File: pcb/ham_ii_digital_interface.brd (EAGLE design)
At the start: 63.5 x 52.7 mm, 21 parts, among them IC1 LM358N, T1 Left Driver, T2 Brake Driver, T3 Right Driver

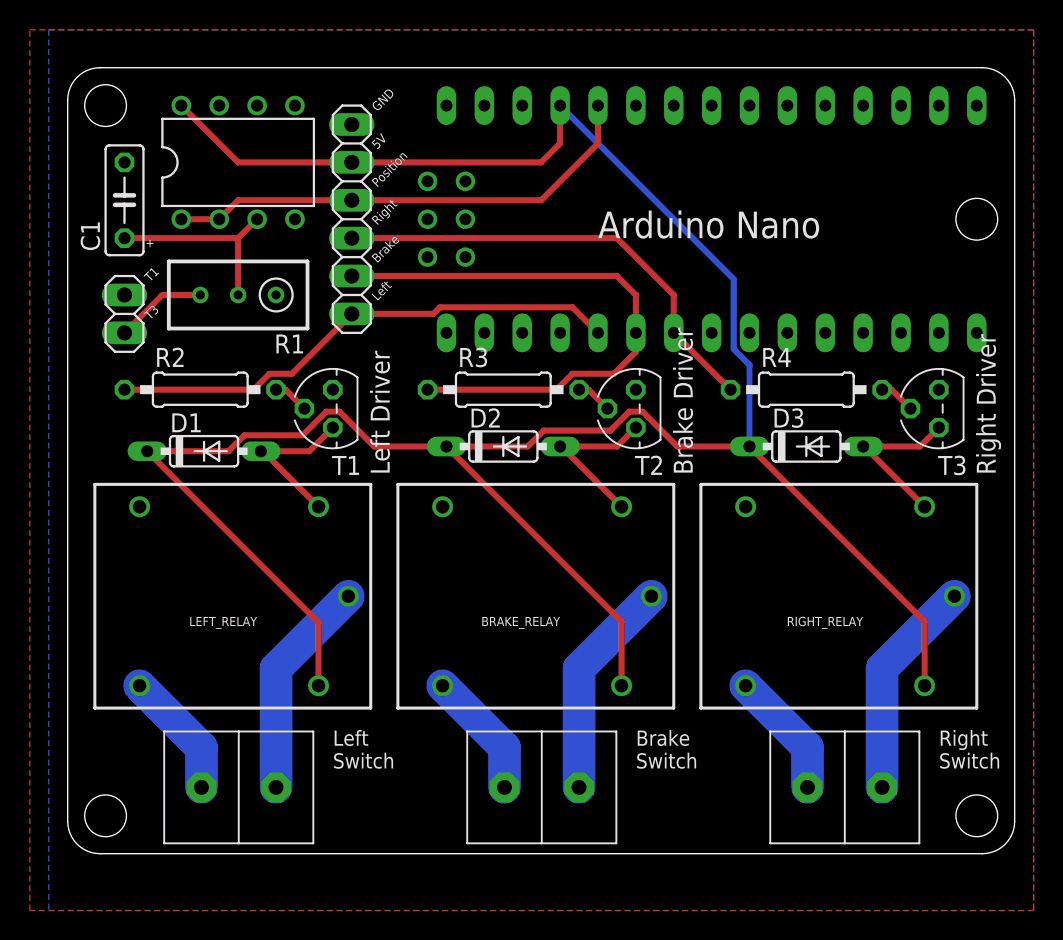
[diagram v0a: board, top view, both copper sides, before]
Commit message: Changed value of C1 and changed C1 to an electrolytic capacitor.
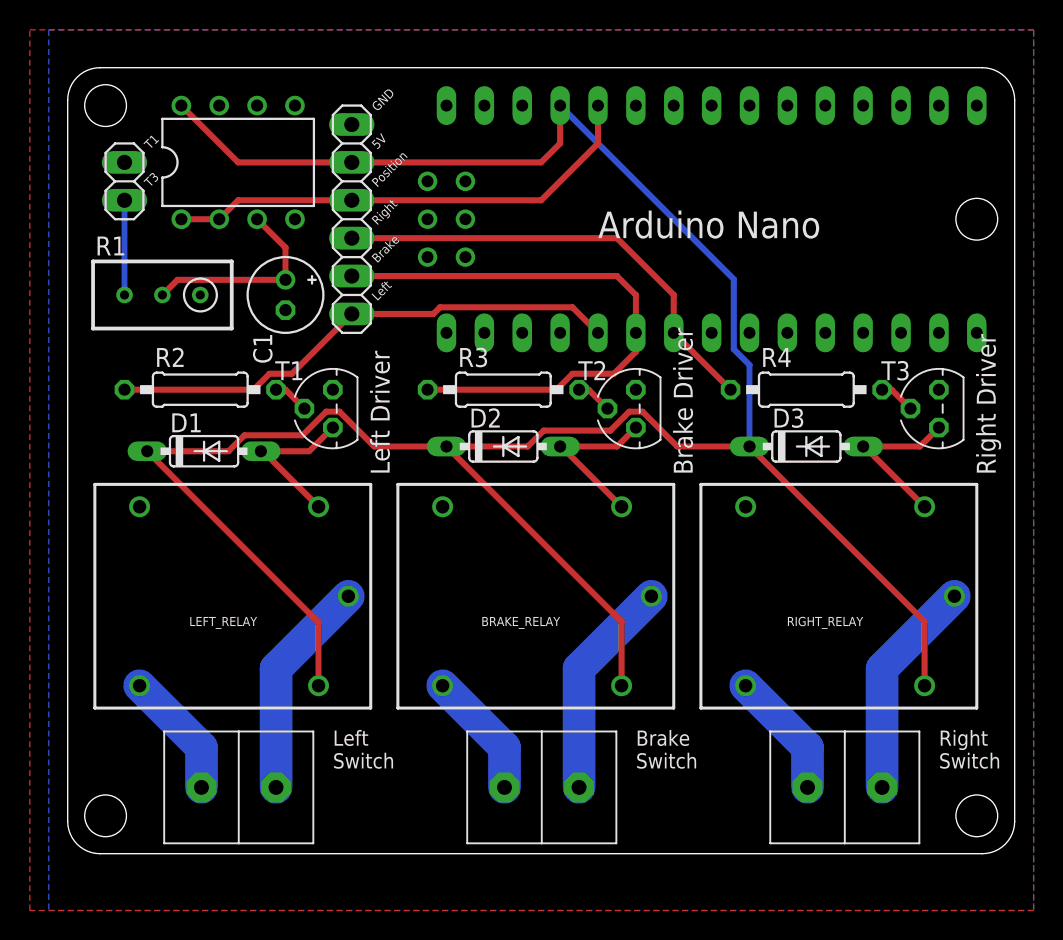
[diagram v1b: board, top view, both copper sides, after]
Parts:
- C1: value 220p -> 1u; device resistor:C050-025X075 -> resistor:E2-5
- moved C1 12.5 mm to (14.6, 37.5), turned to 270 degrees
- moved JP1 8.89 mm to (3.81, 45.1)
- moved R1 5.08 mm to (6.35, 37.5)
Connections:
- net GND: now also C1.-; no longer C1.2
- net N$1: now also C1.+; no longer C1.1
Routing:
- net HAMII_TERMINAL_3: track 7.40 -> 6.35 mm
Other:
- board text added: "HAM II Digital Interface Ed Sandor, KC9ZQW ewsandor@gmail.com Rev: 2017-04-22"
- board text removed: "+"
- board text removed: "HAM II Digital Interface Ed Sandor, KC9ZQW ewsandor@gmail.com Rev: 2017-04-19"
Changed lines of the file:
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@@
 Ed Sandor, KC9ZQW
 ewsandor@gmail.com
-Rev: 2017-04-19</text>
+Rev: 2017-04-22</text>
 <text x="35.56" y="41.275" size="1.778" layer="21">Arduino Nano</text>
 <hole x="2.54" y="50.165" drill="2.8"/>
@@
 <text x="58.42" y="5.715" size="1.016" layer="21">Right
 Switch</text>
-<text x="5.08" y="38.735" size="0.6096" layer="21" rot="R45" align="top-left">T1</text>
-<text x="5.08" y="36.195" size="0.6096" layer="21" rot="R45" align="top-left">T3</text>
+<text x="5.08" y="47.625" size="0.6096" layer="21" rot="R45" align="top-left">T1</text>
+<text x="5.08" y="45.085" size="0.6096" layer="21" rot="R45" align="top-left">T3</text>
 <text x="20.32" y="50.165" size="0.6096" layer="21" rot="R45" align="top-left">GND</text>
 <text x="20.32" y="47.625" size="0.6096" layer="21" rot="R45" align="top-left">5V</text>
@@
 <text x="20.32" y="40.005" size="0.6096" layer="21" rot="R45" align="top-left">Brake</text>
 <text x="20.32" y="37.465" size="0.6096" layer="21" rot="R45" align="top-left">Left</text>
-<text x="5.207" y="41.275" size="0.6096" layer="21" align="top-left">+</text>
 <wire x1="0" y1="50.536978125" x2="0" y2="2.168021875" width="0" layer="20"/>
 <wire x1="0" y1="2.168021875" x2="2.168021875" y2="0" width="0" layer="20" curve="90"/>
@@
 </class>
 </classes>
-<designrules name="default">
+<designrules name="default *">
 <description language="de">&lt;b&gt;EAGLE Design Rules&lt;/b&gt;
 &lt;p&gt;
@@
 <param name="dpGapFactor" value="2.5"/>
 <param name="checkGrid" value="0"/>
-<param name="checkAngle" value="0"/>
+<param name="checkAngle" value="1"/>
 <param name="checkFont" value="1"/>
 <param name="checkRestrict" value="1"/>
@@
 <attribute name="VALUE" x="7.874" y="45.72" size="1.27" layer="27" ratio="10"/>
 </element>
-<element name="JP1" library="pinhead" package="1X02" value="HAMII" x="3.81" y="36.195" smashed="yes" rot="R90">
-<attribute name="VALUE" x="1.905" y="33.655" size="1.27" layer="27" rot="R90"/>
+<element name="JP1" library="pinhead" package="1X02" value="HAMII" x="3.81" y="45.085" smashed="yes" rot="R90">
+<attribute name="VALUE" x="1.905" y="42.545" size="1.27" layer="27" rot="R90"/>
 </element>
 <element name="U$1" library="Arduino-clone" package="NANO" value="NANO" x="34.29" y="40.005" rot="R270"/>
-<element name="R1" library="resistor" package="RTRIM3296W" value="2M" x="11.43" y="37.465" smashed="yes" rot="R90">
-<attribute name="NAME" x="15.93" y="34.815" size="1.27" layer="25" rot="R180"/>
+<element name="R1" library="resistor" package="RTRIM3296W" value="2M" x="6.35" y="37.465" smashed="yes" rot="R90">
+<attribute name="NAME" x="1.85" y="40.115" size="1.27" layer="25"/>
 </element>
 <element name="LEFT_RELAY" library="SRD-05VDC-SL-C" package="SRD-05VDC-SL-C" value="RELAYPTH" x="11.43" y="17.145" rot="R180"/>
@@
 <element name="U$7" library="Terminal Block Connector" package="DBCONN-1X2" value="DBCONN-1X2" x="52.07" y="4.445" rot="R180"/>
 <element name="T1" library="transistor" package="TO92" value="Left Driver" x="17.78" y="29.845" smashed="yes" rot="R90">
-<attribute name="NAME" x="19.685" y="26.67" size="1.27" layer="25" ratio="10" rot="R180"/>
+<attribute name="NAME" x="15.875" y="33.02" size="1.27" layer="25" ratio="10" rot="R180"/>
 <attribute name="VALUE" x="21.59" y="25.4" size="1.27" layer="21" ratio="10" rot="R90"/>
 </element>
 <element name="T2" library="transistor" package="TO92" value="Brake Driver" x="38.1" y="29.845" smashed="yes" rot="R90">
-<attribute name="NAME" x="40.005" y="26.67" size="1.27" layer="25" ratio="10" rot="R180"/>
+<attribute name="NAME" x="36.195" y="33.02" size="1.27" layer="25" ratio="10" rot="R180"/>
 <attribute name="VALUE" x="41.91" y="25.4" size="1.27" layer="21" ratio="10" rot="R90"/>
 </element>
 <element name="T3" library="transistor" package="TO92" value="Right Driver" x="58.42" y="29.845" smashed="yes" rot="R90">
-<attribute name="NAME" x="60.325" y="26.67" size="1.27" layer="25" ratio="10" rot="R180"/>
+<attribute name="NAME" x="56.515" y="33.02" size="1.27" layer="25" ratio="10" rot="R180"/>
 <attribute name="VALUE" x="62.23" y="25.4" size="1.27" layer="21" ratio="10" rot="R90"/>
 </element>
@@
 <attribute name="VALUE" x="20.32" y="52.07" size="1.27" layer="27" rot="R180"/>
 </element>
-<element name="C1" library="resistor" package="C050-025X075" value="220p" x="3.81" y="43.815" smashed="yes" rot="R90">
-<attribute name="NAME" x="2.159" y="40.386" size="1.27" layer="25" ratio="10" rot="R90"/>
+<element name="C1" library="resistor" package="E2-5" value="1u" x="14.605" y="37.465" smashed="yes" rot="R270">
+<attribute name="NAME" x="12.446" y="34.925" size="1.27" layer="25" ratio="10" rot="R270"/>
 </element>
 </elements>
@@
 <contactref element="T1" pad="1"/>
 <contactref element="JP2" pad="6"/>
-<contactref element="C1" pad="2"/>
+<contactref element="C1" pad="-"/>
 </signal>
 <signal name="ROTOR_POSITION_SIGNAL">
@@
 <contactref element="JP1" pad="1"/>
 <contactref element="R1" pad="3"/>
-<wire x1="8.89" y1="37.465" x2="7.62" y2="37.465" width="0.4064" layer="1"/>
-<wire x1="3.81" y1="34.925" x2="6.35" y2="37.465" width="0.4064" layer="1"/>
-<wire x1="6.35" y1="37.465" x2="8.89" y2="37.465" width="0.4064" layer="1"/>
+<wire x1="3.81" y1="43.815" x2="3.81" y2="37.465" width="0.4064" layer="16"/>
 </signal>
 <signal name="5V">
@@
 <contactref element="IC1" pad="3"/>
 <contactref element="R1" pad="2"/>
-<contactref element="C1" pad="1"/>
-<wire x1="11.43" y1="41.275" x2="3.81" y2="41.275" width="0.4064" layer="1"/>
-<wire x1="12.7" y1="42.545" x2="11.43" y2="41.275" width="0.4064" layer="1"/>
-<wire x1="11.43" y1="41.275" x2="11.43" y2="37.465" width="0.4064" layer="1"/>
+<contactref element="C1" pad="+"/>
+<wire x1="12.7" y1="42.545" x2="14.605" y2="40.64" width="0.4064" layer="1"/>
+<wire x1="14.605" y1="38.481" x2="14.605" y2="40.64" width="0.4064" layer="1"/>
+<wire x1="6.35" y1="37.465" x2="7.366" y2="38.481" width="0.4064" layer="1"/>
+<wire x1="7.366" y1="38.481" x2="14.605" y2="38.481" width="0.4064" layer="1"/>
 </signal>
 <signal name="N$2">

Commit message: Improved trace routing.
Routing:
- net ROTOR_POSITION_SIGNAL: track 32.6 -> 34.5 mm
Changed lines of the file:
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@@
 <wire x1="35.56" y1="47.625" x2="31.75" y2="43.815" width="0.4064" layer="1"/>
 <wire x1="31.75" y1="43.815" x2="19.05" y2="43.815" width="0.4064" layer="1"/>
+<wire x1="35.56" y1="50.165" x2="35.56" y2="48.26" width="0.4064" layer="16"/>
 </signal>
 <signal name="HAMII_TERMINAL_3">
@@
 <wire x1="5.334" y1="26.9875" x2="16.82" y2="15.5015" width="0.4064" layer="1"/>
 <wire x1="16.82" y1="15.5015" x2="16.82" y2="11.265" width="0.4064" layer="1"/>
-<wire x1="45.72" y1="32.7713625" x2="45.72" y2="27.305" width="0.4064" layer="16"/>
-<wire x1="44.6596" y1="33.8317625" x2="45.72" y2="32.7713625" width="0.4064" layer="16"/>
-<wire x1="33.02" y1="50.165" x2="44.6596" y2="38.5254" width="0.4064" layer="16"/>
-<wire x1="44.6596" y1="38.5254" x2="44.6596" y2="33.8317625" width="0.4064" layer="16"/>
 <wire x1="33.02" y1="50.165" x2="33.02" y2="47.625" width="0.4064" layer="1"/>
 <wire x1="33.02" y1="47.625" x2="31.75" y2="46.355" width="0.4064" layer="1"/>
 <wire x1="31.75" y1="46.355" x2="19.05" y2="46.355" width="0.4064" layer="1"/>
+<wire x1="33.02" y1="50.165" x2="33.02" y2="45.72" width="0.4064" layer="16"/>
+<wire x1="41.91" y1="36.83" x2="33.02" y2="45.72" width="0.4064" layer="16"/>
+<wire x1="45.72" y1="27.305" x2="41.91" y2="31.115" width="0.4064" layer="16"/>
+<wire x1="41.91" y1="31.115" x2="41.91" y2="36.83" width="0.4064" layer="16"/>
 </signal>
 <signal name="N$1">

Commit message: Minor improvments before ordering first run
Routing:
- net ROTOR_POSITION_SIGNAL: track 34.5 -> 32.6 mm
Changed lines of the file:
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@@
 <element name="T1" library="transistor" package="TO92" value="Left Driver" x="17.78" y="29.845" smashed="yes" rot="R90">
 <attribute name="NAME" x="15.875" y="33.02" size="1.27" layer="25" ratio="10" rot="R180"/>
-<attribute name="VALUE" x="21.59" y="25.4" size="1.27" layer="21" ratio="10" rot="R90"/>
+<attribute name="VALUE" x="20.955" y="27.305" size="0.8128" layer="21" ratio="10" rot="R90"/>
 </element>
 <element name="T2" library="transistor" package="TO92" value="Brake Driver" x="38.1" y="29.845" smashed="yes" rot="R90">
 <attribute name="NAME" x="36.195" y="33.02" size="1.27" layer="25" ratio="10" rot="R180"/>
-<attribute name="VALUE" x="41.91" y="25.4" size="1.27" layer="21" ratio="10" rot="R90"/>
+<attribute name="VALUE" x="41.275" y="26.67" size="0.8128" layer="21" ratio="10" rot="R90"/>
 </element>
 <element name="T3" library="transistor" package="TO92" value="Right Driver" x="58.42" y="29.845" smashed="yes" rot="R90">
 <attribute name="NAME" x="56.515" y="33.02" size="1.27" layer="25" ratio="10" rot="R180"/>
-<attribute name="VALUE" x="62.23" y="25.4" size="1.27" layer="21" ratio="10" rot="R90"/>
+<attribute name="VALUE" x="61.595" y="26.67" size="0.8128" layer="21" ratio="10" rot="R90"/>
 </element>
 <element name="R2" library="resistor" package="0207/10" value="1K" x="8.89" y="31.115" smashed="yes">
@@
 </element>
 <element name="C1" library="resistor" package="E2-5" value="1u" x="14.605" y="37.465" smashed="yes" rot="R270">
-<attribute name="NAME" x="12.446" y="34.925" size="1.27" layer="25" ratio="10" rot="R270"/>
+<attribute name="NAME" x="13.335" y="40.894" size="1.27" layer="25" ratio="10" rot="R180"/>
 </element>
 </elements>
@@
 <contactref element="JP2" pad="6"/>
 <contactref element="C1" pad="-"/>
+<via x="29.845" y="45.085" extent="1-16" drill="0.7" shape="square"/>
 </signal>
 <signal name="ROTOR_POSITION_SIGNAL">
@@
 <contactref element="JP2" pad="4"/>
 <wire x1="10.16" y1="42.545" x2="11.43" y2="43.815" width="0.4064" layer="1"/>
-<wire x1="19.05" y1="43.815" x2="11.43" y2="43.815" width="0.4064" layer="1"/>
+<wire x1="11.43" y1="43.815" x2="19.05" y2="43.815" width="0.4064" layer="1"/>
 <contactref element="U$1" pad="A7"/>
-<wire x1="35.56" y1="50.165" x2="35.56" y2="47.625" width="0.4064" layer="1"/>
-<wire x1="35.56" y1="47.625" x2="31.75" y2="43.815" width="0.4064" layer="1"/>
-<wire x1="31.75" y1="43.815" x2="19.05" y2="43.815" width="0.4064" layer="1"/>
-<wire x1="35.56" y1="50.165" x2="35.56" y2="48.26" width="0.4064" layer="16"/>
+<wire x1="19.05" y1="43.815" x2="31.75" y2="43.815" width="0.4064" layer="1"/>
+<wire x1="35.56" y1="47.625" x2="35.56" y2="50.165" width="0.4064" layer="1"/>
+<wire x1="31.75" y1="43.815" x2="35.56" y2="47.625" width="0.4064" layer="1"/>
 </signal>
 <signal name="HAMII_TERMINAL_3">
@@
 <wire x1="33.02" y1="47.625" x2="31.75" y2="46.355" width="0.4064" layer="1"/>
 <wire x1="31.75" y1="46.355" x2="19.05" y2="46.355" width="0.4064" layer="1"/>
-<wire x1="33.02" y1="50.165" x2="33.02" y2="45.72" width="0.4064" layer="16"/>
-<wire x1="41.91" y1="36.83" x2="33.02" y2="45.72" width="0.4064" layer="16"/>
+<wire x1="33.02" y1="50.165" x2="33.02" y2="47.625" width="0.4064" layer="16"/>
+<wire x1="41.91" y1="38.735" x2="33.02" y2="47.625" width="0.4064" layer="16"/>
 <wire x1="45.72" y1="27.305" x2="41.91" y2="31.115" width="0.4064" layer="16"/>
-<wire x1="41.91" y1="31.115" x2="41.91" y2="36.83" width="0.4064" layer="16"/>
+<wire x1="41.91" y1="31.115" x2="41.91" y2="38.735" width="0.4064" layer="16"/>
 </signal>
 <signal name="N$1">

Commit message: Fixed issue discovered after receiving print of PCB.  The NO and NC pins on the SRD-05VDC-SL-C schematic symbol are reveresed resulting in incorrect functionality.  Trace must be cut on NC pin and a jumper must be added for NO to correct previous revision of PCB.  Correction has been made to PCB, noted on schematic.
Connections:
- net N$3: now also LEFT_RELAY.SWCLOSED; no longer LEFT_RELAY.SWOPEN
- net N$5: now also BRAKE_RELAY.SWCLOSED; no longer BRAKE_RELAY.SWOPEN
- net N$7: now also RIGHT_RELAY.SWCLOSED; no longer RIGHT_RELAY.SWOPEN
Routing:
- net N$7: track 8.54 -> 20.5 mm
- net N$5: track 8.54 -> 20.5 mm
- net N$3: track 8.54 -> 20.5 mm
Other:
- board text added: "HAM II Digital Interface Ed Sandor, KC9ZQW ewsandor@gmail.com Rev: 2017-05-05"
- board text removed: "HAM II Digital Interface Ed Sandor, KC9ZQW ewsandor@gmail.com Rev: 2017-04-22"
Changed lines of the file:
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@@
 Ed Sandor, KC9ZQW
 ewsandor@gmail.com
-Rev: 2017-04-22</text>
+Rev: 2017-05-05</text>
 <text x="35.56" y="41.275" size="1.778" layer="21">Arduino Nano</text>
 <hole x="2.54" y="50.165" drill="2.8"/>
@@
 <wire x1="13.97" y1="12.415" x2="13.97" y2="4.445" width="2.1844" layer="16"/>
 </signal>
-<signal name="N$3">
-<contactref element="LEFT_RELAY" pad="SWOPEN"/>
-<contactref element="U$5" pad="P1"/>
-<wire x1="4.82" y1="11.265" x2="8.97" y2="7.115" width="2.1844" layer="16"/>
-<wire x1="8.97" y1="7.115" x2="8.97" y2="4.445" width="2.1844" layer="16"/>
-</signal>
 <signal name="N$4">
 <contactref element="BRAKE_RELAY" pad="SWCOMMON"/>
@@
 <wire x1="34.29" y1="12.415" x2="34.29" y2="4.445" width="2.1844" layer="16"/>
 </signal>
-<signal name="N$5">
-<contactref element="BRAKE_RELAY" pad="SWOPEN"/>
-<contactref element="U$6" pad="P1"/>
-<wire x1="25.14" y1="11.265" x2="29.29" y2="7.115" width="2.1844" layer="16"/>
-<wire x1="29.29" y1="7.115" x2="29.29" y2="4.445" width="2.1844" layer="16"/>
-</signal>
 <signal name="N$6">
 <contactref element="RIGHT_RELAY" pad="SWCOMMON"/>
@@
 <wire x1="59.46" y1="17.265" x2="54.61" y2="12.415" width="2.1844" layer="16"/>
 <wire x1="54.61" y1="12.415" x2="54.61" y2="4.445" width="2.1844" layer="16"/>
-</signal>
-<signal name="N$7">
-<contactref element="RIGHT_RELAY" pad="SWOPEN"/>
-<contactref element="U$7" pad="P1"/>
-<wire x1="45.46" y1="11.265" x2="49.61" y2="7.115" width="2.1844" layer="16"/>
-<wire x1="49.61" y1="7.115" x2="49.61" y2="4.445" width="2.1844" layer="16"/>
 </signal>
 <signal name="N$8">
@@
 <wire x1="13.0975" y1="26.9875" x2="12.954" y2="26.9875" width="0.4064" layer="1"/>
 </signal>
+<signal name="N$3">
+<contactref element="LEFT_RELAY" pad="SWCLOSED"/>
+<contactref element="U$5" pad="P1"/>
+<wire x1="4.82" y1="23.265" x2="8.97" y2="19.115" width="2.1844" layer="16"/>
+<wire x1="8.97" y1="19.115" x2="8.97" y2="4.445" width="2.1844" layer="16"/>
+</signal>
+<signal name="N$5">
+<contactref element="BRAKE_RELAY" pad="SWCLOSED"/>
+<contactref element="U$6" pad="P1"/>
+<wire x1="25.14" y1="23.265" x2="29.29" y2="19.115" width="2.1844" layer="16"/>
+<wire x1="29.29" y1="19.115" x2="29.29" y2="4.445" width="2.1844" layer="16"/>
+</signal>
+<signal name="N$7">
+<contactref element="RIGHT_RELAY" pad="SWCLOSED"/>
+<contactref element="U$7" pad="P1"/>
+<wire x1="45.46" y1="23.265" x2="49.61" y2="19.115" width="2.1844" layer="16"/>
+<wire x1="49.61" y1="19.115" x2="49.61" y2="4.445" width="2.1844" layer="16"/>
+</signal>
 </signals>
